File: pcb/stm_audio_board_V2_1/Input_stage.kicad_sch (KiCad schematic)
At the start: 19 parts, among them U4 OP275

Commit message: fixes in pcb
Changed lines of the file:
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@@
     (stroke (width 0) (type default))
+  )
+  (text_box "NOTE: \n1. The input is level is to high, lower gain is needed\n2. The input filter is too low with R5 and C20. New values needed.\nThe high frequencies are cut down."
+    (at 87.63 29.21 0) (size 57.15 16.51)
+    (stroke (width 0) (type default))
+    (fill (type none))
+    (effects (font (size 1.27 1.27)) (justify left top))
   )
   (global_label "ADC1N" (shape input) (at 219.71 72.39 0) (fields_autoplaced)

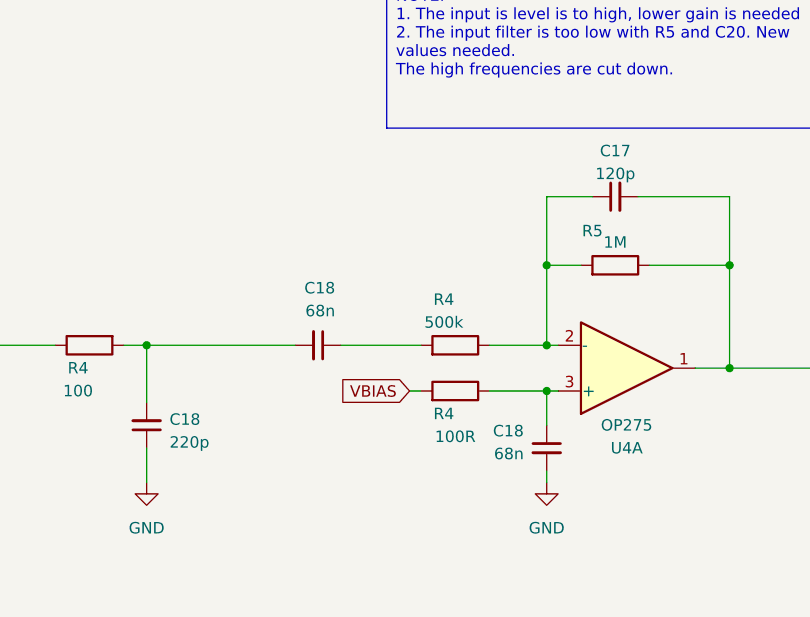
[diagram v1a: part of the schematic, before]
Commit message: audo_board v2_1 output stage is reworked
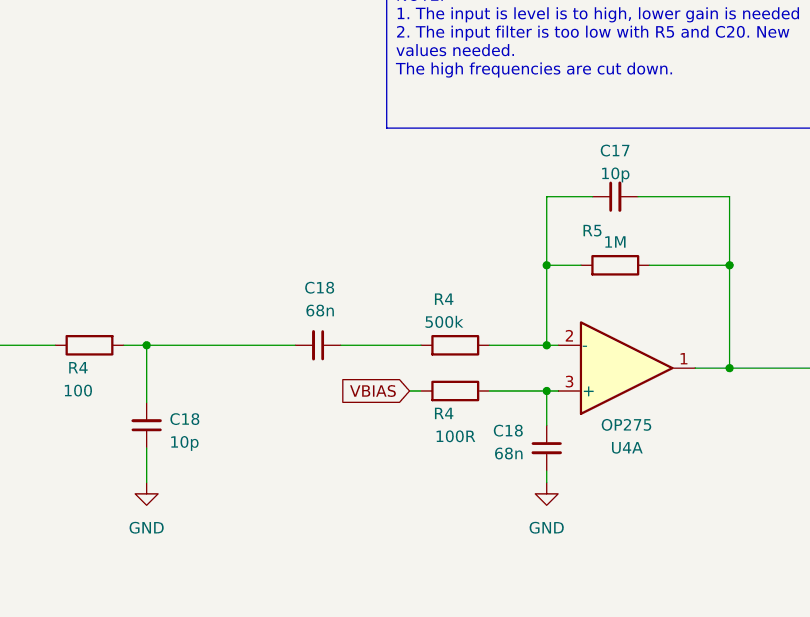
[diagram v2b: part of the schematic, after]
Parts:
- C17: value 120p -> 10p
- C18: value 220p -> 10p
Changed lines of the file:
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@@
       (effects (font (size 1.27 1.27)))
     )
-    (property "Value" "120p" (at 113.0363 50.8 90)
+    (property "Value" "10p" (at 113.0363 50.8 90)
       (effects (font (size 1.27 1.27)))
     )
@@
       (effects (font (size 1.27 1.27)) (justify right))
     )
-    (property "Value" "220p" (at 63.5 80.6386 0)
+    (property "Value" "10p" (at 63.5 80.6386 0)
       (effects (font (size 1.27 1.27)) (justify right))
     )
